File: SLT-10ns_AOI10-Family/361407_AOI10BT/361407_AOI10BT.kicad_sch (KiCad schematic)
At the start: 21 parts, among them T1 T_DB, T2 T_DB

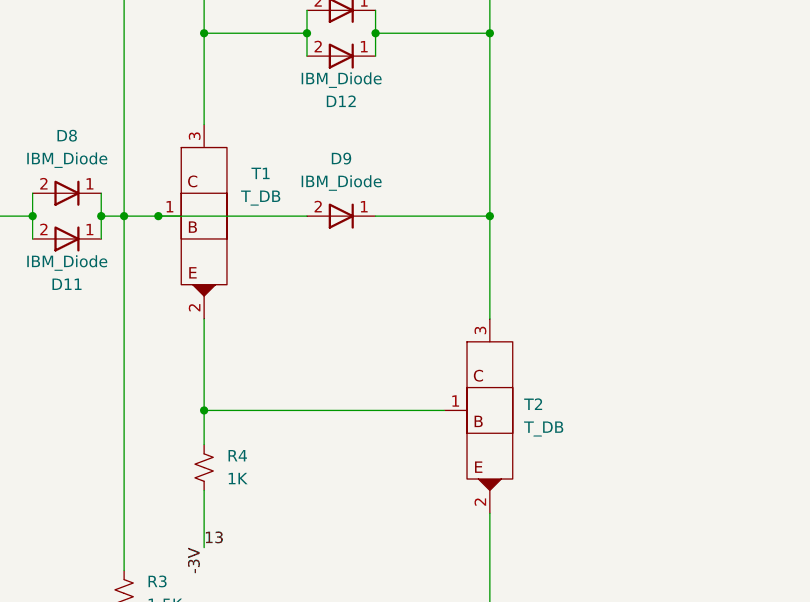
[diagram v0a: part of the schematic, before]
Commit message: Finished off the SLT-30 family of parts, started on the SLT-700 family. Changed labeling of transistors and diodes in all schematics, but have yet to update all the pdf files. This is a TODO...
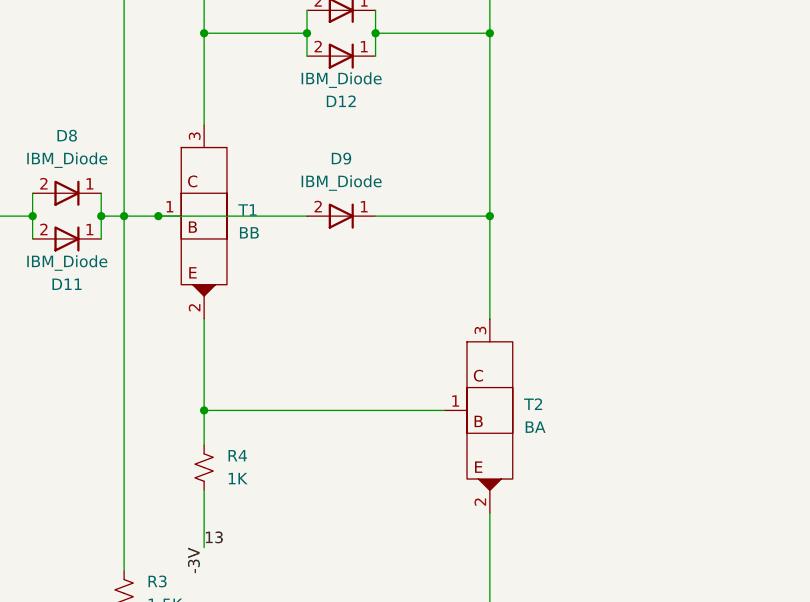
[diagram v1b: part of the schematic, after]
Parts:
- T1: value T_DB -> BB
- T2: value T_DB -> BA
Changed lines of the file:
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@@
   (symbol (lib_id "IBM_SLT-SLD:T_DB") (at 120.65 93.98 0) (unit 1)
     (in_bom yes) (on_board yes) (fields_autoplaced)
-    (property "Reference" "T1" (id 0) (at 127 89.281 0))
-    (property "Value" "T_DB" (id 1) (at 127 91.821 0))
+    (property "Reference" "T1" (id 0) (at 124.46 93.3449 0)
+      (effects (font (size 1.27 1.27)) (justify left))
+    )
+    (property "Value" "BB" (id 1) (at 124.46 95.8849 0)
+      (effects (font (size 1.27 1.27)) (justify left))
+    )
     (property "Footprint" "Package_DFN_QFN:Diodes_DFN1006-3" (id 2) (at 120.65 93.98 0)
       (effects (font (size 1.27 1.27)) hide)
@@
       (effects (font (size 1.27 1.27)) (justify left))
     )
-    (property "Value" "T_DB" (id 1) (at 156.21 117.4749 0)
+    (property "Value" "BA" (id 1) (at 156.21 117.4749 0)
       (effects (font (size 1.27 1.27)) (justify left))
     )
@@
     )
     (path "/95303cff-6932-4821-b7e1-1e8ef06881c6"
-      (reference "T1") (unit 1) (value "T_DB") (footprint "Package_DFN_QFN:Diodes_DFN1006-3")
+      (reference "T1") (unit 1) (value "BB") (footprint "Package_DFN_QFN:Diodes_DFN1006-3")
     )
     (path "/aca742d5-d20c-41e7-9ac8-8b36b22cfba4"
-      (reference "T2") (unit 1) (value "T_DB") (footprint "Package_DFN_QFN:Diodes_DFN1006-3")
+      (reference "T2") (unit 1) (value "BA") (footprint "Package_DFN_QFN:Diodes_DFN1006-3")
     )
     (path "/98cf94aa-9a14-4efb-965e-894e721f61fd"
